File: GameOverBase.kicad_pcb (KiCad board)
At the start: 4 copper layers, 50 x 30 mm, 48 parts, among them J1 USB_C_DEALON-USB-US31-106, J2 Serial Port, J3 add-on conn, Q1 PMN48XP, SW1 SW_DIP_x08, SW2 boot, SW3 Reset, U1 ESP32-WROOM-E, U2 4021, U3 MCP73831-2ACI-OT, U4 XC6210B332MR

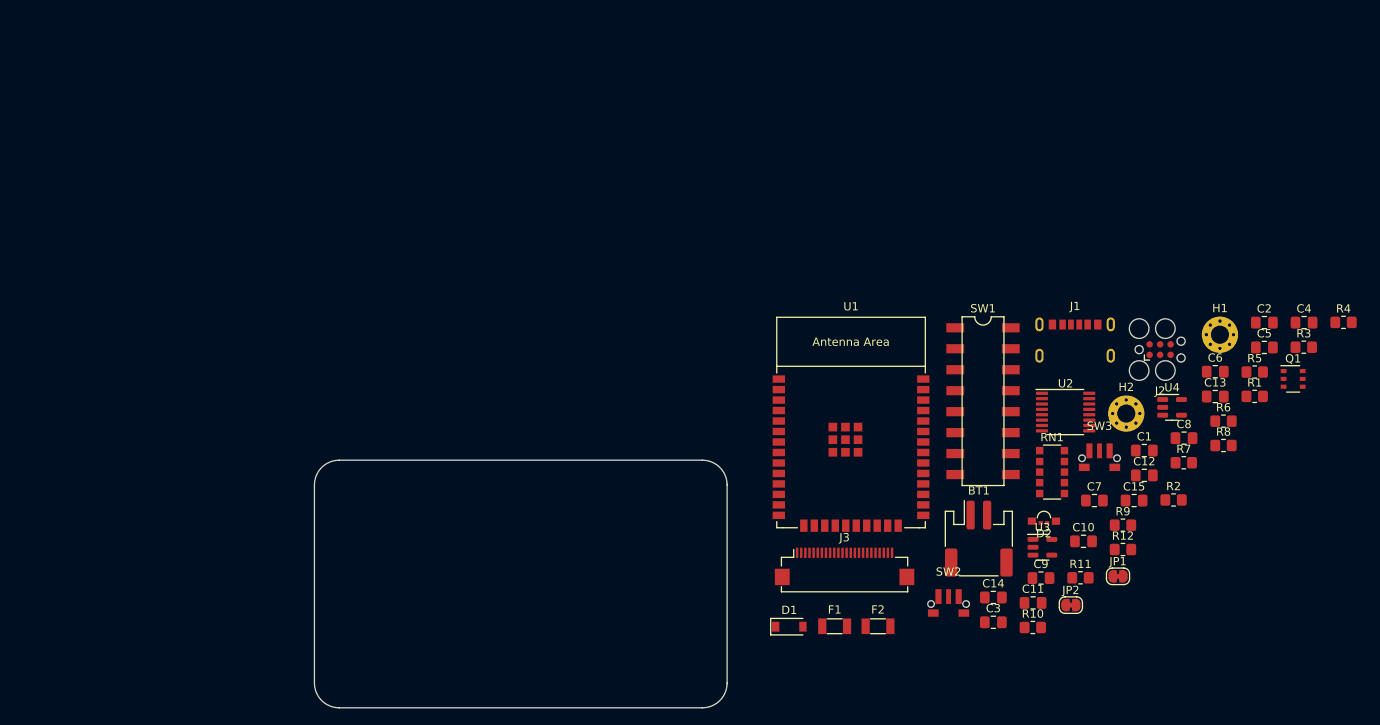
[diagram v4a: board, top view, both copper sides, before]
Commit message: Roughly groups together components for the power circuit
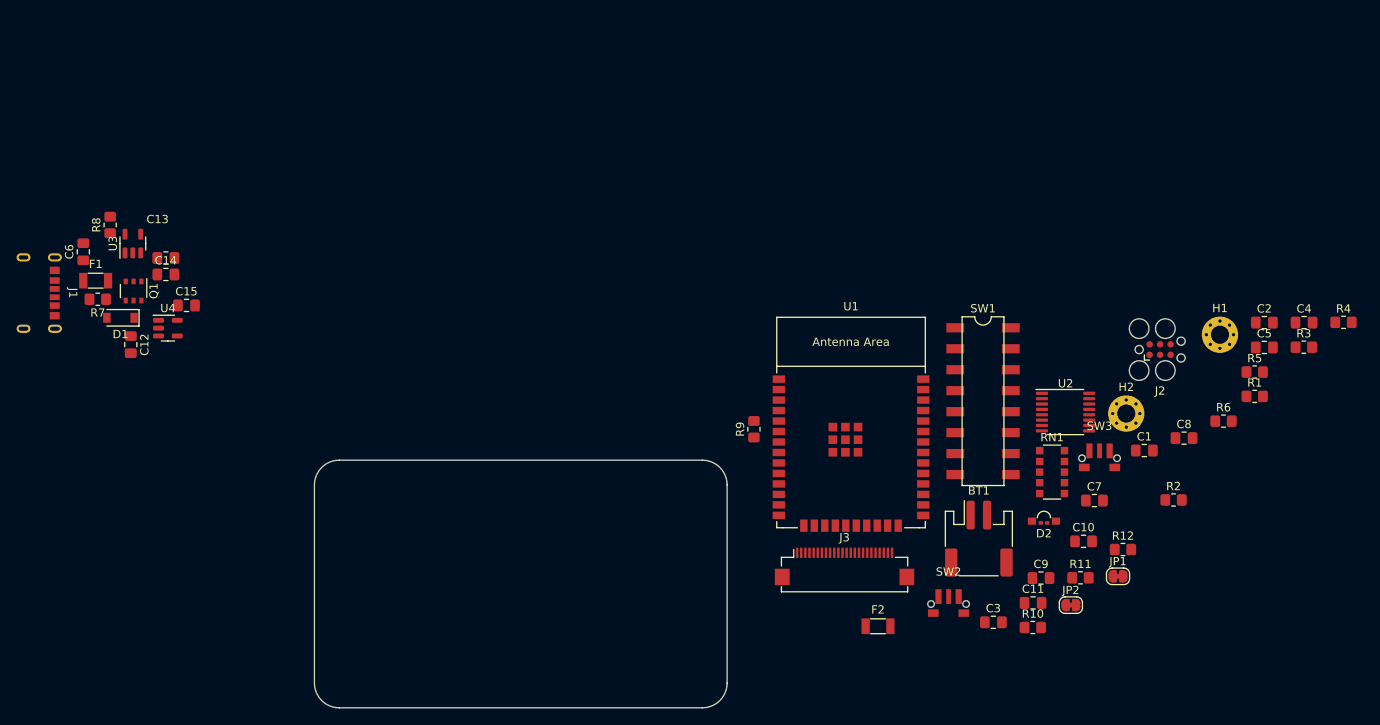
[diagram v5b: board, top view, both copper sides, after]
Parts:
- moved Q1 140.9 mm to (98.1, 59.5), turned to -90 degrees
- moved C6 137.9 mm to (92.0, 54.8), turned to 90 degrees
- moved R8 137.5 mm to (95.2, 51.5), turned to 90 degrees
- moved R7 133.1 mm to (93.8, 60.5), turned to 180 degrees
- moved C13 128.2 mm to (102.0, 55.5)
- moved J1 126.6 mm to (85.8, 59.8), turned to -90 degrees
- moved C12 123.8 mm to (97.8, 66.0), turned to -90 degrees
- moved U4 122.0 mm to (102.2, 64.0)
- moved C15 117.2 mm to (104.5, 61.2)
- moved U3 116.2 mm to (98.0, 53.8), turned to 90 degrees
- moved C14 107.6 mm to (102.0, 57.5)
- moved F1 98.8 mm to (93.5, 58.2)
- moved D1 89.3 mm to (96.5, 62.8), turned to 180 degrees
- moved R9 46.2 mm to (173.2, 76.2), turned to 90 degrees

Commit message: Adds extra capacitance to the VBUS decoupling
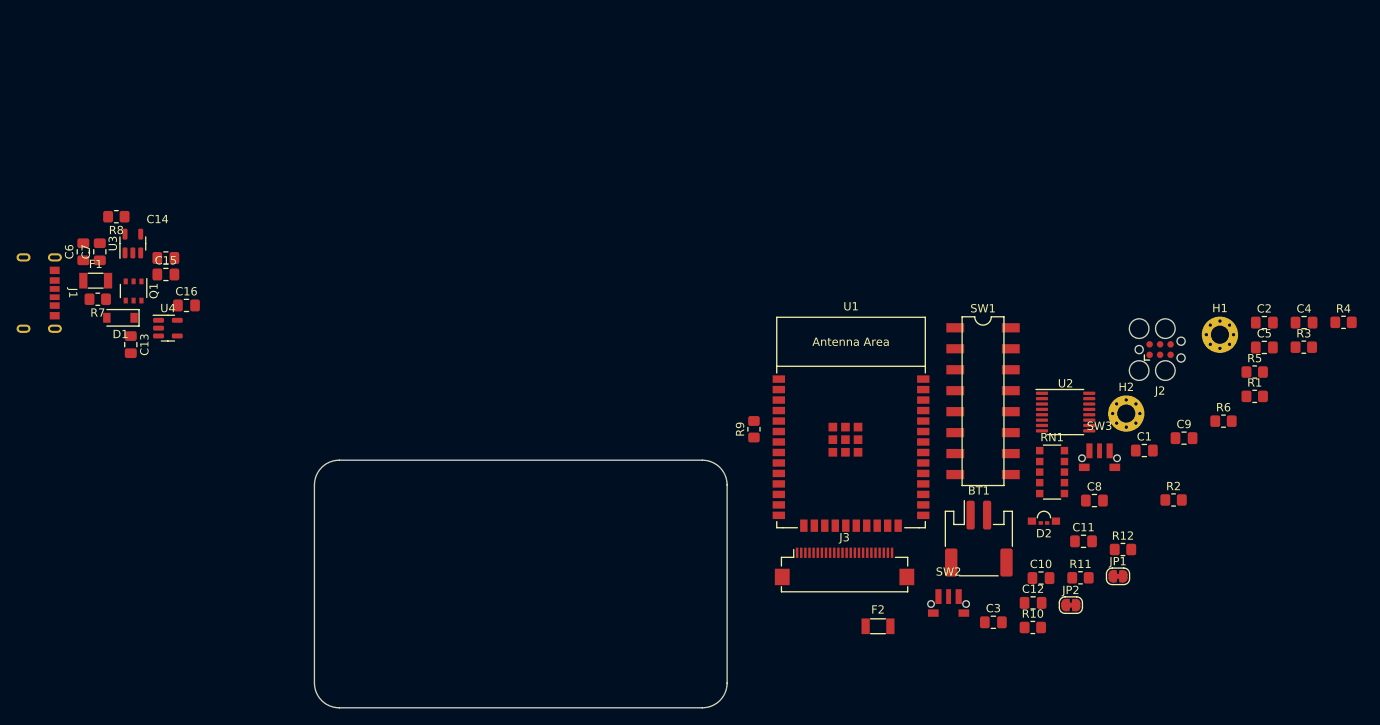
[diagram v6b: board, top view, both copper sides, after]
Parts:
- added C7: 10µF, Capacitor_SMD:C_0805_2012Metric_Pad1.18x1.45mm_HandSolder, F.Cu at (94.0, 54.8)
- moved R8 1.25 mm to (96.0, 50.5), turned to 180 degrees
- renumbered C9 to C10, C10 to C11, C11 to C12, C12 to C13, C13 to C14, C14 to C15, C15 to C16, C7 to C8, C8 to C9
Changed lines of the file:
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@@
     (property "Sheetname" "")
     (attr smd)
-    (fp_text reference "C7" (at 0 -1.68) (layer "F.SilkS")
+    (fp_text reference "C8" (at 0 -1.68) (layer "F.SilkS")
         (effects (font (size 1 1) (thickness 0.15)))
     )
@@
     (property "Sheetname" "")
     (attr smd)
-    (fp_text reference "C8" (at 0 -1.68) (layer "F.SilkS")
+    (fp_text reference "C9" (at 0 -1.68) (layer "F.SilkS")
         (effects (font (size 1 1) (thickness 0.15)))
     )
@@
     (property "Sheetname" "")
     (attr smd)
-    (fp_text reference "C13" (at -1 -4.68) (layer "F.SilkS")
+    (fp_text reference "C14" (at -1 -4.68) (layer "F.SilkS")
         (effects (font (size 1 1) (thickness 0.15)))
     )
@@
     (property "Sheetname" "")
     (attr smd)
-    (fp_text reference "C15" (at 0 -1.68) (layer "F.SilkS")
+    (fp_text reference "C16" (at 0 -1.68) (layer "F.SilkS")
         (effects (font (size 1 1) (thickness 0.15)))
     )
@@
     (property "Sheetname" "")
     (attr smd)
-    (fp_text reference "C11" (at 0 -1.68) (layer "F.SilkS")
+    (fp_text reference "C12" (at 0 -1.68) (layer "F.SilkS")
         (effects (font (size 1 1) (thickness 0.15)))
     )
@@
     (property "Sheetname" "")
     (attr smd)
-    (fp_text reference "C12" (at 0 -1.68 90) (layer "F.SilkS")
+    (fp_text reference "C13" (at 0 -1.68 90) (layer "F.SilkS")
         (effects (font (size 1 1) (thickness 0.15)))
     )
@@
     (property "Sheetname" "")
     (attr smd)
-    (fp_text reference "C9" (at 0 -1.68) (layer "F.SilkS")
+    (fp_text reference "C10" (at 0 -1.68) (layer "F.SilkS")
         (effects (font (size 1 1) (thickness 0.15)))
     )
@@
   )
   (footprint "Resistor_SMD:R_0805_2012Metric_Pad1.20x1.40mm_HandSolder" (layer "F.Cu")
-    (at 95.25 51.5 90)
+    (at 96 50.5 180)
     (descr "Resistor SMD 0805 (2012 Metric), square (rectangular) end terminal, IPC_7351 nominal with elongated pad for handsoldering. (Body size source: IPC-SM-782 page 72, https://www.pcb-3d.com/wordpress/wp-content/uploads/ipc-sm-782a_amendment_1_and_2.pdf), generated with kicad-footprint-generator")
     (tags "resistor handsolder")
@@
     (property "Sheetname" "")
     (attr smd)
-    (fp_text reference "R8" (at 0 -1.65 90) (layer "F.SilkS")
-        (effects (font (size 1 1) (thickness 0.15)))
-    )
-    (fp_text value "5.1kΩ *" (at 0 1.65 90) (layer "F.Fab")
-        (effects (font (size 1 1) (thickness 0.15)))
-    )
-    (fp_text user "${REFERENCE}" (at 0 0 90) (layer "F.Fab")
+    (fp_text reference "R8" (at 0 -1.65) (layer "F.SilkS")
+        (effects (font (size 1 1) (thickness 0.15)))
+    )
+    (fp_text value "5.1kΩ *" (at 0 1.65) (layer "F.Fab")
+        (effects (font (size 1 1) (thickness 0.15)))
+    )
+    (fp_text user "${REFERENCE}" (at 0 0) (layer "F.Fab")
         (effects (font (size 0.5 0.5) (thickness 0.08)))
     )
@@
     (fp_line (start 1 0.625) (end -1 0.625)
       (stroke (width 0.1) (type solid)) (layer "F.Fab"))
-    (pad "1" smd roundrect (at -1 0 90) (size 1.2 1.4) (layers "F.Cu" "F.Paste" "F.Mask") (roundrect_rratio 0.208333)
+    (pad "1" smd roundrect (at -1 0 180) (size 1.2 1.4) (layers "F.Cu" "F.Paste" "F.Mask") (roundrect_rratio 0.208333)
       (net 44 "Net-(U3-PROG)") (pintype "passive"))
-    (pad "2" smd roundrect (at 1 0 90) (size 1.2 1.4) (layers "F.Cu" "F.Paste" "F.Mask") (roundrect_rratio 0.208333)
+    (pad "2" smd roundrect (at 1 0 180) (size 1.2 1.4) (layers "F.Cu" "F.Paste" "F.Mask") (roundrect_rratio 0.208333)
       (net 2 "GND") (pintype "passive"))
     (model "${KICAD6_3DMODEL_DIR}/Resistor_SMD.3dshapes/R_0805_2012Metric.wrl"
@@
   )
   (footprint "Capacitor_SMD:C_0805_2012Metric_Pad1.18x1.45mm_HandSolder" (layer "F.Cu")
+    (at 94 54.75 90)
+    (descr "Capacitor SMD 0805 (2012 Metric), square (rectangular) end terminal, IPC_7351 nominal with elongated pad for handsoldering. (Body size source: IPC-SM-782 page 76, https://www.pcb-3d.com/wordpress/wp-content/uploads/ipc-sm-782a_amendment_1_and_2.pdf, https://docs.google.com/spreadsheets/d/1BsfQQcO9C6DZCsRaXUlFlo91Tg2WpOkGARC1WS5S8t0/edit?usp=sharing), generated with kicad-footprint-generator")
+    (tags "capacitor handsolder")
+    (property "Sheetfile" "GameOverBase.kicad_sch")
+    (property "Sheetname" "")
+    (attr smd)
+    (fp_text reference "C7" (at 0 -1.68 90) (layer "F.SilkS")
+        (effects (font (size 1 1) (thickness 0.15)))
+    )
+    (fp_text value "10µF" (at 0 1.68 90) (layer "F.Fab")
+        (effects (font (size 1 1) (thickness 0.15)))
+    )
+    (fp_text user "${REFERENCE}" (at 0 0 90) (layer "F.Fab")
+        (effects (font (size 0.5 0.5) (thickness 0.08)))
+    )
+    (fp_line (start -0.261252 -0.735) (end 0.261252 -0.735)
+      (stroke (width 0.12) (type solid)) (layer "F.SilkS"))
+    (fp_line (start -0.261252 0.735) (end 0.261252 0.735)
+      (stroke (width 0.12) (type solid)) (layer "F.SilkS"))
+    (fp_line (start -1.88 -0.98) (end 1.88 -0.98)
+      (stroke (width 0.05) (type solid)) (layer "F.CrtYd"))
+    (fp_line (start -1.88 0.98) (end -1.88 -0.98)
+      (stroke (width 0.05) (type solid)) (layer "F.CrtYd"))
+    (fp_line (start 1.88 -0.98) (end 1.88 0.98)
+      (stroke (width 0.05) (type solid)) (layer "F.CrtYd"))
+    (fp_line (start 1.88 0.98) (end -1.88 0.98)
+      (stroke (width 0.05) (type solid)) (layer "F.CrtYd"))
+    (fp_line (start -1 -0.625) (end 1 -0.625)
+      (stroke (width 0.1) (type solid)) (layer "F.Fab"))
+    (fp_line (start -1 0.625) (end -1 -0.625)
+      (stroke (width 0.1) (type solid)) (layer "F.Fab"))
+    (fp_line (start 1 -0.625) (end 1 0.625)
+      (stroke (width 0.1) (type solid)) (layer "F.Fab"))
+    (fp_line (start 1 0.625) (end -1 0.625)
+      (stroke (width 0.1) (type solid)) (layer "F.Fab"))
+    (pad "1" smd roundrect (at -1.0375 0 90) (size 1.175 1.45) (layers "F.Cu" "F.Paste" "F.Mask") (roundrect_rratio 0.212766)
+      (net 7 "Net-(J1-VBUS)") (pintype "passive"))
+    (pad "2" smd roundrect (at 1.0375 0 90) (size 1.175 1.45) (layers "F.Cu" "F.Paste" "F.Mask") (roundrect_rratio 0.212766)
+      (net 2 "GND") (pintype "passive"))
+    (model "${KICAD6_3DMODEL_DIR}/Capacitor_SMD.3dshapes/C_0805_2012Metric.wrl"
+      (offset (xyz 0 0 0))
+      (scale (xyz 1 1 1))
+      (rotate (xyz 0 0 0))
+    )
+  )
+  (footprint "Capacitor_SMD:C_0805_2012Metric_Pad1.18x1.45mm_HandSolder" (layer "F.Cu")
     (at 235.09 66.34)
     (descr "Capacitor SMD 0805 (2012 Metric), square (rectangular) end terminal, IPC_7351 nominal with elongated pad for handsoldering. (Body size source: IPC-SM-782 page 76, https://www.pcb-3d.com/wordpress/wp-content/uploads/ipc-sm-782a_amendment_1_and_2.pdf, https://docs.google.com/spreadsheets/d/1BsfQQcO9C6DZCsRaXUlFlo91Tg2WpOkGARC1WS5S8t0/edit?usp=sharing), generated with kicad-footprint-generator")
@@
     (property "Sheetname" "")
     (attr smd)
-    (fp_text reference "C10" (at 0 -1.68) (layer "F.SilkS")
+    (fp_text reference "C11" (at 0 -1.68) (layer "F.SilkS")
         (effects (font (size 1 1) (thickness 0.15)))
     )
@@
     (property "Sheetname" "")
     (attr smd)
-    (fp_text reference "C14" (at 0 -1.68) (layer "F.SilkS")
-        (effects (font (size 1 1) (thickness 0.15)))
-    )
+    (fp_text reference "C15" (at 0 -1.68) (layer "F.SilkS")
+        (effects (font (size 1 1) (thickness 0.15)))
+    )
